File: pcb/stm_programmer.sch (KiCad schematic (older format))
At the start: 37 parts

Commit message: Un-fucked library references
Fixed bad paths in sym/fp-lib-table
Deleted "rescue" library
Removed references to rescue library
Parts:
- U?: symbol Ventilator-rescue:STM32F103CxTx-RespiraWorks -> RespiraWorks:STM32F103CxTx
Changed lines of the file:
@@
 $EndDescr
 $Comp
-L Ventilator-rescue:STM32F103CxTx-RespiraWorks U?
+L RespiraWorks:STM32F103CxTx U?
 U 1 1 5FEEC109
 P 7750 3700
@@
 $EndComp
 $Comp
-L Ventilator-rescue:+5V_USB-RespiraWorks #PWR?
+L RespiraWorks:+5V_USB #PWR?
 U 1 1 5FFFC08C
 P 1550 2250
@@
 	1550 2250 1550 2300
 $Comp
-L Ventilator-rescue:+5V_USB-RespiraWorks #PWR?
+L RespiraWorks:+5V_USB #PWR?
 U 1 1 5FFFF9F0
 P 2300 1250
@@
 $EndComp
 $Comp
-L Ventilator-rescue:+3.3V_Ctrl-RespiraWorks #PWR?
+L RespiraWorks:+3.3V_Ctrl #PWR?
 U 1 1 6000178D
 P 1750 1350
@@
 $EndComp
 $Comp
-L Ventilator-rescue:+3.3V_Ctrl-RespiraWorks #PWR?
+L RespiraWorks:+3.3V_Ctrl #PWR?
 U 1 1 60001E93
 P 2100 4900
@@
 $EndComp
 $Comp
-L Ventilator-rescue:+3.3V_Ctrl-RespiraWorks #PWR?
+L RespiraWorks:+3.3V_Ctrl #PWR?
 U 1 1 6000A757
 P 2100 6400
@@
 $EndComp
 $Comp
-L Ventilator-rescue:+3.3V_Ctrl-RespiraWorks #PWR?
+L RespiraWorks:+3.3V_Ctrl #PWR?
 U 1 1 6000EE0D
 P 5450 4250
@@
 $EndComp
 $Comp
-L Ventilator-rescue:+3.3V_Ctrl-RespiraWorks #PWR?
+L RespiraWorks:+3.3V_Ctrl #PWR?
 U 1 1 6001037F
 P 6550 1550
@@
 $EndComp
 $Comp
-L Ventilator-rescue:+3.3V_Ctrl-RespiraWorks #PWR?
+L RespiraWorks:+3.3V_Ctrl #PWR?
 U 1 1 6001165E
 P 7950 1450
@@
 Connection ~ 7950 1450
 $Comp
-L Ventilator-rescue:+3.3V_Ctrl-RespiraWorks #PWR?
+L RespiraWorks:+3.3V_Ctrl #PWR?
 U 1 1 60013B92
 P 9350 2650
@@
 	8450 2750 8800 2750
 $Comp
-L Ventilator-rescue:+3.3V_Ctrl-RespiraWorks #PWR?
+L RespiraWorks:+3.3V_Ctrl #PWR?
 U 1 1 6006697C
 P 4250 1850

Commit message: prior stash
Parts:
- removed C? (x5): 100nF 100V X7R, RespiraWorks_Std:C_0603_1608Metric, symbol Device:C
- removed C? (x2): 20pF 50V NP0, RespiraWorks_Std:C_0603_1608Metric, symbol Device:C
- removed D?: Red, symbol Device:LED_ALT
- removed D?: Green, symbol Device:LED_ALT
- removed J?: USB B micro, symbol Connector:USB_B_Micro
- removed J?: Backup debug in for cycle controller, symbol Connector_Generic:Conn_01x06
- removed J?: Debug in for ST-LINK, symbol Connector_Generic:Conn_01x06
- removed JP? (x5): Jumper_NC_Small, RespiraWorks_Std:SolderJumper-2_P1.3mm_Bridged_RoundedPad1.0x1.5mm, symbol Device:Jumper_NC_Small
- removed JP?: Jumper_NO_Small, RespiraWorks_Std:SolderJumper-2_P1.3mm_Open_RoundedPad1.0x1.5mm, symbol Device:Jumper_NO_Small
- removed Q?: MMBT2222A, RespiraWorks_Std:SOT-23, symbol Device:Q_NPN_BCE
- removed R? (x3): 100K 1%, RespiraWorks_Std:R_0603_1608Metric, symbol Device:R
- removed R? (x2): 100 1%, RespiraWorks_Std:R_0603_1608Metric, symbol Device:R
- removed R? (x2): 0, RespiraWorks_Std:R_0603_1608Metric, symbol Device:R
- removed R?: 1.5K 1%, RespiraWorks_Std:R_0603_1608Metric, symbol Device:R
- removed R? (x2): 10K 1%, RespiraWorks_Std:R_0603_1608Metric, symbol Device:R
- removed R?: 36K 1%, RespiraWorks_Std:R_0603_1608Metric, symbol Device:R
- removed R? (x2): 1K 1%, RespiraWorks_Std:R_0603_1608Metric, symbol Device:R
- removed R? (x2): 4.7K 1%, RespiraWorks_Std:R_0603_1608Metric, symbol Device:R
- removed R?: DNP, RespiraWorks_Std:R_0603_1608Metric, symbol Device:R
- removed U?: STM32F103CBT6, RespiraWorks_Std:LQFP-48_7x7mm_P0.5mm, symbol RespiraWorks:STM32F103CxTx
- removed Y?: 8 Mhz, RespiraWorks_Std:Crystal_SMD_HC49-SD, symbol Device:Crystal
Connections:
- no-connect marks 15 -> 0
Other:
- note removed: "Board identity"
- note removed: "Cut jumpers to use\nan external programmer\nto program the cycle\ncontroller instead of this\nbuilt-in programmer"
- note removed: "Ext. voltage sense; unsure why\nset @ 2.5V"
- note removed: "High: can draw 100 mA max. from USB\n (will always self-power successfully)\nLow: can draw 300 mA max. from USB\n (needs to negotiate power draw)"
- note removed: "Unsure of purpose"

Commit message: combined schs
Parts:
- added C? (x5): 100nF 100V X7R, RespiraWorks_Std:C_0603_1608Metric, symbol Device:C
- added C? (x2): 20pF 50V NP0, RespiraWorks_Std:C_0603_1608Metric, symbol Device:C
- added D?: Red, symbol Device:LED_ALT
- added D?: Green, symbol Device:LED_ALT
- added J?: USB B micro, symbol Connector:USB_B_Micro
- added J?: Backup debug in for cycle controller, symbol Connector_Generic:Conn_01x06
- added J?: Debug in for ST-LINK, symbol Connector_Generic:Conn_01x06
- added JP? (x5): Jumper_NC_Small, RespiraWorks_Std:SolderJumper-2_P1.3mm_Bridged_RoundedPad1.0x1.5mm, symbol Device:Jumper_NC_Small
- added JP?: Jumper_NO_Small, RespiraWorks_Std:SolderJumper-2_P1.3mm_Open_RoundedPad1.0x1.5mm, symbol Device:Jumper_NO_Small
- added Q?: MMBT2222A, RespiraWorks_Std:SOT-23, symbol Device:Q_NPN_BCE
- added R? (x3): 100K 1%, RespiraWorks_Std:R_0603_1608Metric, symbol Device:R
- added R? (x2): 100 1%, RespiraWorks_Std:R_0603_1608Metric, symbol Device:R
- added R? (x2): 0, RespiraWorks_Std:R_0603_1608Metric, symbol Device:R
- added R?: 1.5K 1%, RespiraWorks_Std:R_0603_1608Metric, symbol Device:R
- added R? (x2): 10K 1%, RespiraWorks_Std:R_0603_1608Metric, symbol Device:R
- added R?: 36K 1%, RespiraWorks_Std:R_0603_1608Metric, symbol Device:R
- added R? (x2): 1K 1%, RespiraWorks_Std:R_0603_1608Metric, symbol Device:R
- added R? (x2): 4.7K 1%, RespiraWorks_Std:R_0603_1608Metric, symbol Device:R
- added R?: DNP, RespiraWorks_Std:R_0603_1608Metric, symbol Device:R
- added U?: STM32F103CBT6, RespiraWorks_Std:LQFP-48_7x7mm_P0.5mm, symbol RespiraWorks:STM32F103CxTx
- added Y?: 8 Mhz, RespiraWorks_Std:Crystal_SMD_HC49-SD, symbol Device:Crystal
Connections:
- new net: R?.2, U?.2 (PC13)
- new net: R?.1, U?.25 (PB12)
- new net: R?.2, U?.3 (PC14/OSC32_IN)
- new net: D?.1 (K), D?.2 (A), U?.30 (PA9)
- new net: JP?.1, JP?.2, U?.39 (PB3/JTDO)
- new net: R?.1, U?.44 (BOOT0)
- new net: C?.2, U?.5 (PD0/OSCIN), Y?.1
- new net: C?.2, U?.6 (PD1/OSCOUT), Y?.2
- new net: J?.2 (D-), R?.1
- new net: J?.3 (D+), R?.1, R?.2
- new net: J?.4 (ID), R?.2
- new net: Q?.3 (E), R?.2
- new net: Q?.1 (B), R?.1, R?.2, R?.2
- new net: D?.1 (K), R?.1
- new net: D?.2 (A), R?.2
- new net +3.3V_Ctrl: C?.2, C?.2, C?.2, C?.2, J?.1 (Pin_1), J?.1 (Pin_1), JP?.1, Q?.2 (C), R?.1, R?.1, R?.2, U?.1 (VBAT), U?.24 (VDD), U?.36 (VDD), U?.48 (VDD), U?.9 (VDDA)
- new net +5V_USB: J?.1 (VBUS), R?.2
- new net CC_SWCLK: J?.2 (Pin_2), JP?.1
- new net CC_SWCLK_Out: JP?.2, U?.15 (PA5), U?.26 (PB13)
- new net CC_SWDIO: J?.4 (Pin_4), JP?.1
- new net CC_SWDIO_Out: JP?.2, R?.2, U?.27 (PB14)
- new net CC_SWO: J?.6 (Pin_6), JP?.1
- new net CC_SWO_Out: JP?.2, U?.31 (PA10)
- new net GND: C?.1, C?.1, C?.1, C?.1, C?.1, C?.1, C?.1, J?.3 (Pin_3), J?.3 (Pin_3), J?.5 (GND), J?.6 (Pin_6), J?.6 (Shield), JP?.2, R?.1, R?.1, R?.1, R?.1, R?.1, R?.2, R?.2, U?.20 (PB2/BOOT1), U?.23 (VSS), U?.35 (VSS), U?.47 (VSS), U?.8 (VSSA)
- new net Prog_SWCLK: J?.2 (Pin_2), U?.37 (PA14/JTCK/SWCLK)
- new net Prog_SWDIO: J?.4 (Pin_4), U?.34 (PA13/JTMS/SWDIO)
- new net UART_Rx: U?.13 (PA3)
- new net UART_Tx: U?.12 (PA2)
- new net USB_D+: R?.1, U?.33 (PA12)
- new net USB_D-: R?.2, U?.32 (PA11)
- new net VSense: R?.1, R?.2, U?.10 (PA0/WKUP)
- new net ~CC_RST: J?.5 (Pin_5), JP?.1
- new net ~CC_RST_Out: JP?.2, U?.18 (PB0)
- new net ~Prog_RST: C?.2, J?.5 (Pin_5), R?.2, U?.7 (~RST)
- new net ~USB_Pwr_En: U?.28 (PB15)
- new net ~USB_Renum: R?.1, U?.38 (PA15/JTDI)
- no-connect marks 0 -> 15
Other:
- note added: "Board identity"
- note added: "Cut jumpers to use\nan external programmer\nto program the cycle\ncontroller instead of this\nbuilt-in programmer"
- note added: "Ext. voltage sense; unsure why\nset @ 2.5V"
- note added: "High: can draw 100 mA max. from USB\n (will always self-power successfully)\nLow: can draw 300 mA max. from USB\n (needs to negotiate power draw)"
- note added: "Unsure of purpose"

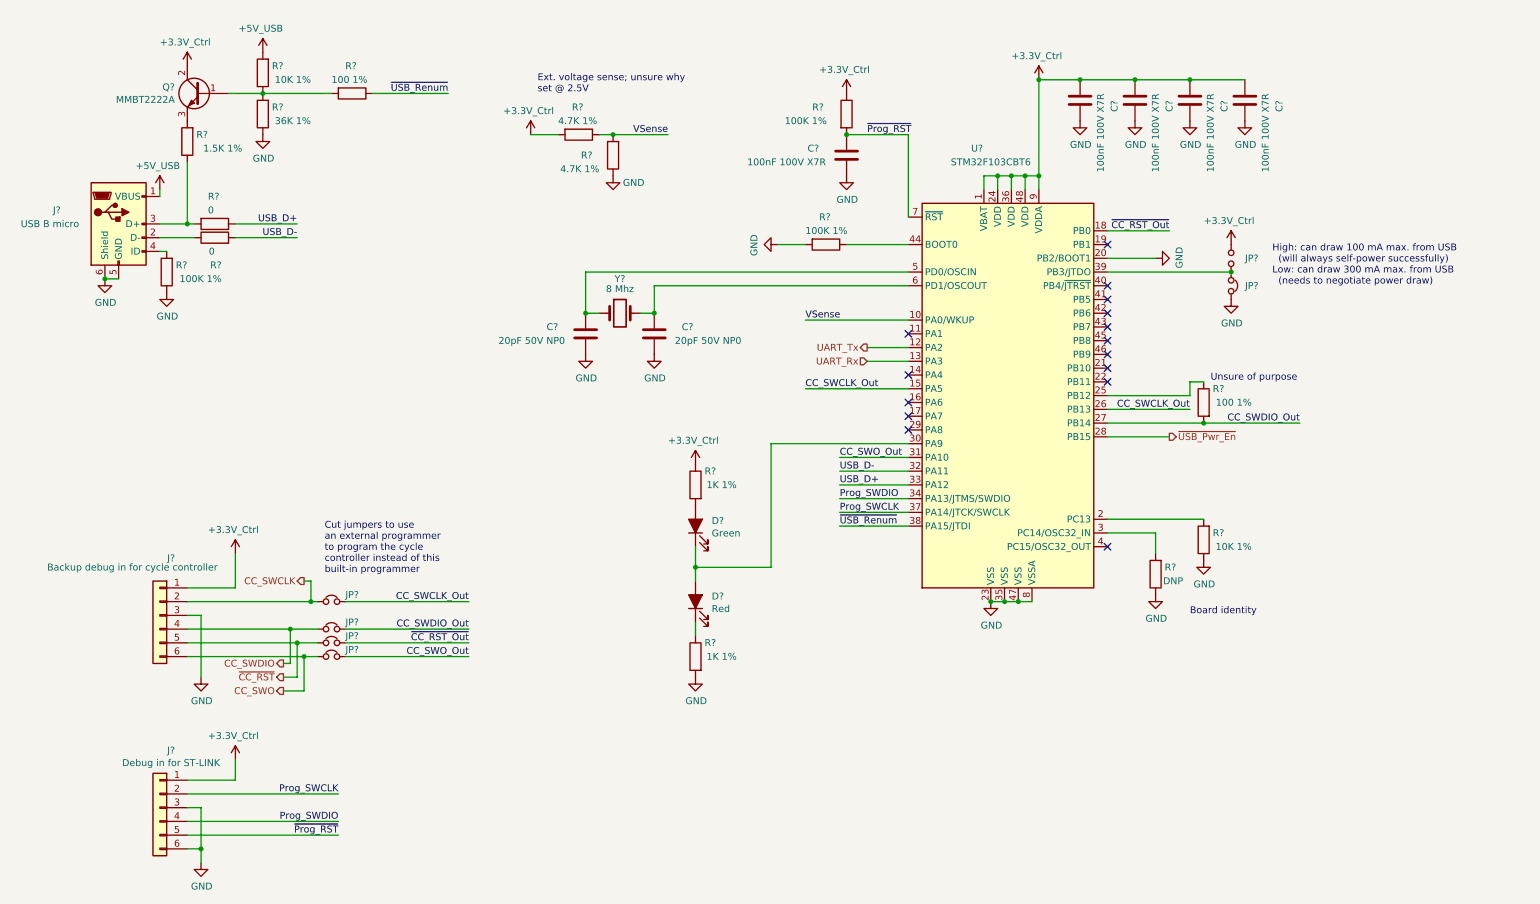
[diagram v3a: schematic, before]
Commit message: PCB Rev A: Switch ~Signal inversion to nSignal inversion (#984)
* adding system monitor ADC

* adding system monitor ADC

* DNP'd external reference and added 0-ohm option resistor to tie VREF to 3.3V supply

* first commit

* Initial commit

* adding system monitor ADC

* DNP'd external reference and added 0-ohm option resistor to tie VREF to 3.3V supply

* changed DNP parameter name to DNP and cleaned up net names

* scrubbed schematic and replaced ~ inversion with nSignalName inversion

* updated inversion markers per convention FPGA_nRST > nRST_FPGA (and similar)

* Minor cleanup

Changed power supply ports from outputs to inputs
Changed ADC's symbol and footprint to point to RespiraWorks libraries

* scrubbed schematic and replaced ~ inversion with nSignalName inversion

* updated inversion markers per convention FPGA_nRST > nRST_FPGA (and similar)

Co-authored-by: neelfirst <neelfirst@gmail.com>
Co-authored-by: neelfirst <neelfirst@users.noreply.github.com>
Co-authored-by: dcstraney <63062249+dcstraney@users.noreply.github.com>
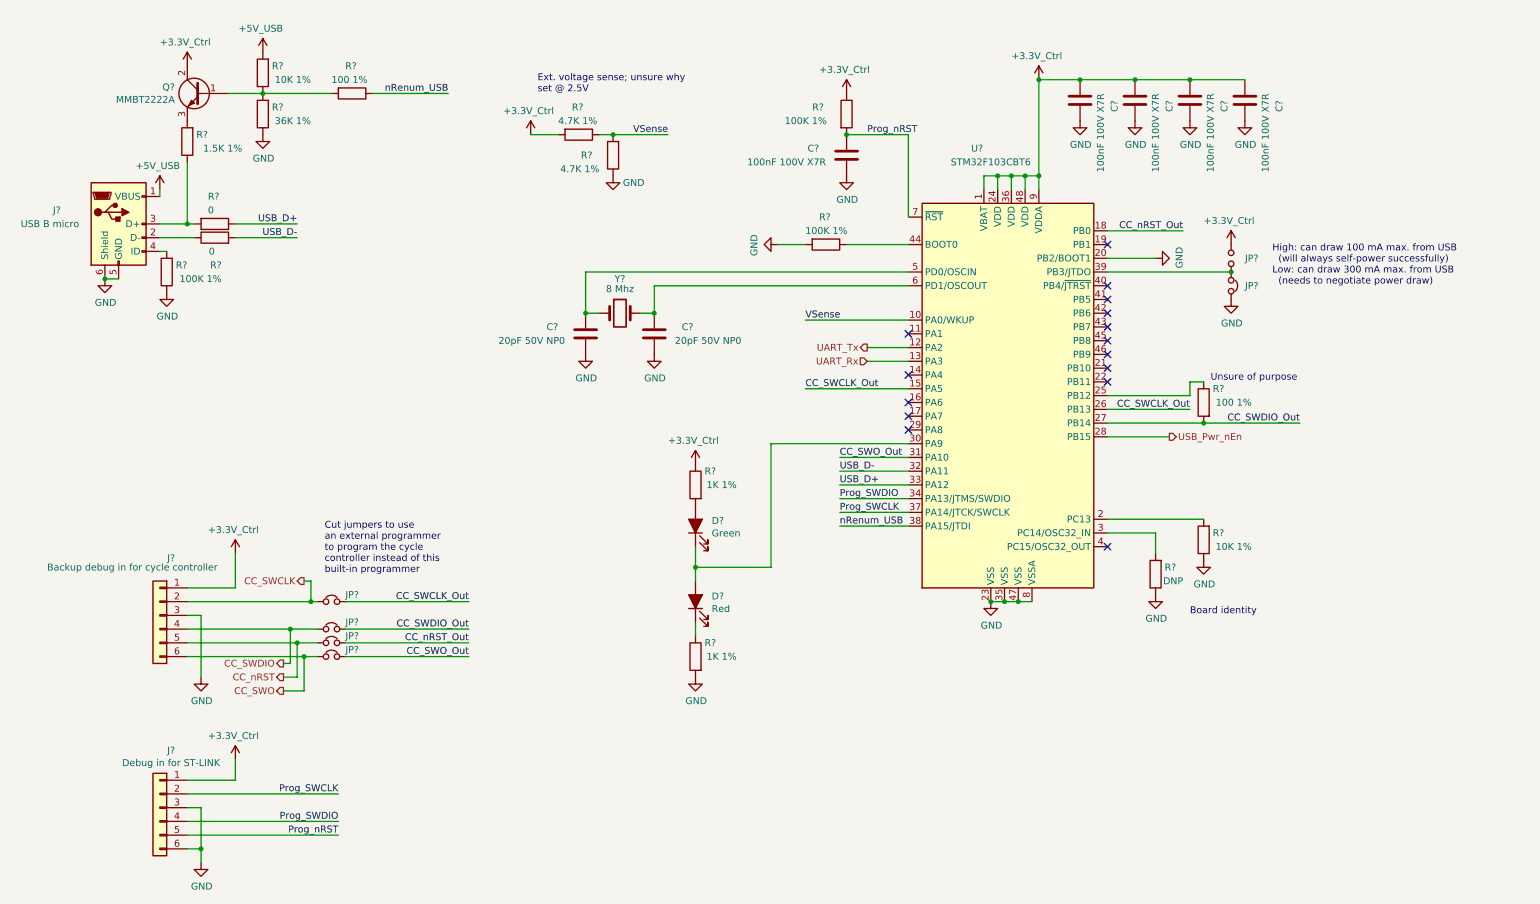
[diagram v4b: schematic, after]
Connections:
- net ~CC_RST renamed CC_nRST
- net ~CC_RST_Out renamed CC_nRST_Out
- net ~Prog_RST renamed Prog_nRST
- net ~USB_Pwr_En renamed USB_Pwr_nEn
- net ~USB_Renum renamed nRenum_USB
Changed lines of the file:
@@
 U 1 1 5FF1A7AE
 P 1250 2500
+AR Path="/5FF1A7AE" Ref="J?"  Part="1"
+AR Path="/5FCD4D85/5FF1A7AE" Ref="J?"  Part="1"
 F 0 "J?" H 800 2600 50  0000 C CNN
 F 1 "USB B micro" H 750 2500 50  0000 C CNN
@@
 	2800 1550 2300 1550
 Text Label 3650 1550 2    50   ~ 0
-~USB_Renum
+nRenum_USB
 Wire Wire Line
 	3100 1550 3650 1550
@@
 	7000 4700 6500 4700
 Text Label 6500 4700 0    50   ~ 0
-~USB_Renum
+nRenum_USB
 $Comp
 L Connector_Generic:Conn_01x06 J?
@@
 CC_SWDIO_Out
 Text Label 3800 5550 2    50   ~ 0
-~CC_RST_Out
+CC_nRST_Out
 Text Label 3800 5650 2    50   ~ 0
 CC_SWO_Out
@@
 Text Label 9850 3950 2    50   ~ 0
 CC_SWDIO_Out
-Wire Wire Line
-	8450 2550 8900 2550
-Text Label 8900 2550 2    50   ~ 0
-~CC_RST_Out
+Text Label 9000 2550 2    50   ~ 0
+CC_nRST_Out
 Wire Wire Line
 	7000 4200 6500 4200
@@
 Prog_SWCLK
 Text Label 6700 1850 0    50   ~ 0
-~Prog_RST
+Prog_nRST
 $Comp
 L Connector_Generic:Conn_01x06 J?
@@
 Prog_SWDIO
 Text Label 2850 6950 2    50   ~ 0
-~Prog_RST
+Prog_nRST
 Wire Wire Line
 	1750 7050 1850 7050
@@
 CC_SWDIO
 Text HLabel 2450 5800 0    50   Output ~ 0
-~CC_RST
+CC_nRST
 Text HLabel 2450 5900 0    50   Output ~ 0
 CC_SWO
@@
 	8450 4050 8900 4050
 Text HLabel 8900 4050 2    50   Output ~ 0
-~USB_Pwr_En
+USB_Pwr_nEn
 Text Label 5250 1850 2    50   ~ 0
 VSense
@@
 Wire Wire Line
 	8450 3850 9050 3850
+Wire Wire Line
+	8450 2550 9000 2550
 $EndSCHEMATC
